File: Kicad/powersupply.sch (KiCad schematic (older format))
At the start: 19 parts, among them J801 Jack 2/6.3mm, Q801 BC546, Q802 BC556, U801 DC-DC Module, U802 MAX1615, U803 TLV1117 3.3V 1A

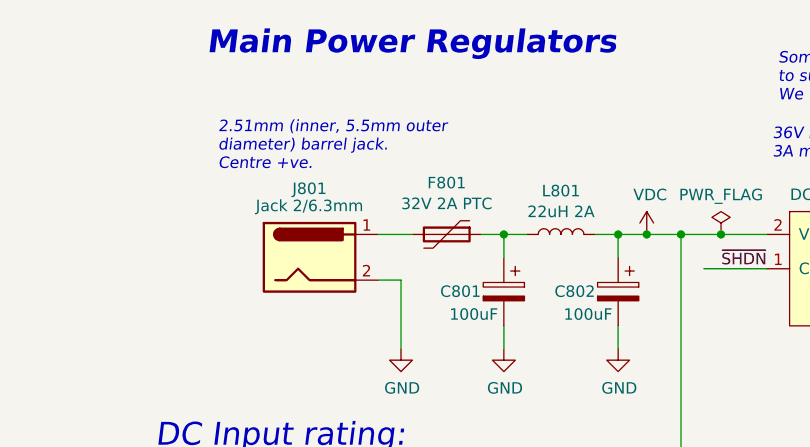
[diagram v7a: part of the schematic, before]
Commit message: Update component values.
Tolerance and Voltage are set to the minimum acceptable. The selected
parts can be better, where a better part is cheaper or has
better availability.

Also dropped R2R DAC tolerance to 1% - 0.5% was overkill. The output
resistor had the wrong value too, which is fixed.
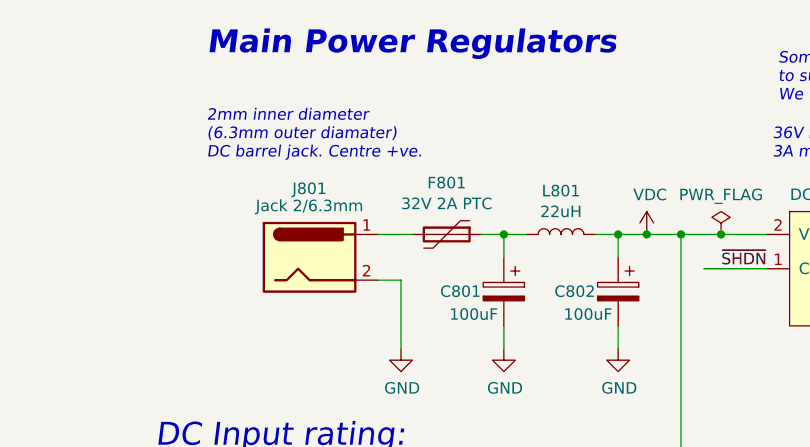
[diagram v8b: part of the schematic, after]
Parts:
- C801, C802: Tolerance (none) -> 20%
- C803: Tolerance (none) -> X5R
- C804, C806, C808: Tolerance (none) -> X5R; Voltage (none) -> 16V
- C805, C807: Tolerance (none) -> X5R; Voltage (none) -> 10V
- L801: value 22uH 2A -> 22uH; Mouser (none) -> 580-13R223C
- Q801: Mouser (none) -> 512-BC546CTA
- Q802: Mouser (none) -> 512-BC556BTF
- R801, R802, R803: Tolerance (none) -> 1%
- U803: Digikey 296-28778-1-ND -> (none); Mouser 595-TLV1117LV33DCYR -> (none)
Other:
- note added: "2mm inner diameter\n(6.3mm outer diamater)\nDC barrel jack. Centre +ve."
- note removed: "2.51mm (inner, 5.5mm outer\ndiameter) barrel jack.\nCentre +ve."
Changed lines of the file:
@@
 Comment4 ""
 $EndDescr
-Text Notes 1975 1850 0    50   Italic 0
-2.51mm (inner, 5.5mm outer\ndiameter) barrel jack.\nCentre +ve.
+Text Notes 1925 1800 0    50   Italic 0
+2mm inner diameter\n(6.3mm outer diamater)\nDC barrel jack. Centre +ve.
 Text Notes 8525 4075 0    50   Italic 0
 Most of our board runs on 3.3V. We expect\nto draw around 100 mA from this 1A linear\nregulator.\n\nNorm. power wasted: (5V - 3.3V) * 0.1A = 0.17W\nMax power wasted: (5V - 3.3V) * 1A = 1.7W\n\nThe LDO is 50 °C/W so at max power,\nit's 85 °C over ambient. Probably best\nto use a heatsink if you want to pull\nover about 250 mA. Or replace with a\n3-terminal switching PSU module.
@@
 F 3 "http://www.ti.com/general/docs/suppproductinfo.tsp?distId=10&gotoUrl=http%3A%2F%2Fwww.ti.com%2Flit%2Fgpn%2Ftlv1117lv" H 7625 3275 50  0001 C CNN
 F 4 "0" H 7525 3525 50  0001 C CNN "DNP"
-F 5 "296-28778-1-ND" H 7525 3525 50  0001 C CNN "Digikey"
+F 5 "~" H 7525 3525 50  0001 C CNN "Digikey"
 F 6 "CPL-REG-LIN-3.3V-1A" H 7525 3525 50  0001 C CNN "MPN"
 F 7 "CPL" H 7525 3525 50  0001 C CNN "Manufacturer"
-F 8 "595-TLV1117LV33DCYR" H 7525 3525 50  0001 C CNN "Mouser"
+F 8 "~" H 7525 3525 50  0001 C CNN "Mouser"
 F 9 "C6186" H 7525 3525 50  0001 C CNN "LCSC Part#"
+F 10 "~" H 7525 3525 50  0001 C CNN "Tolerance"
+F 11 "~" H 7525 3525 50  0001 C CNN "Voltage"
 	1    7525 3525
 	1    0    0    -1
@@
 F 3 "~" H 7875 3775 50  0001 C CNN
 F 4 "0" H 7875 3775 50  0001 C CNN "DNP"
-F 5 "" H 7875 3775 50  0001 C CNN "Digikey"
+F 5 "~" H 7875 3775 50  0001 C CNN "Digikey"
 F 6 "CPL-CAP-X7R-0805-1UF-25V" H 7875 3775 50  0001 C CNN "MPN"
 F 7 "CPL" H 7875 3775 50  0001 C CNN "Manufacturer"
 F 8 "C28323" H 7875 3775 50  0001 C CNN "LCSC Part#"
+F 9 "X5R" H 7875 3775 50  0001 C CNN "Tolerance"
+F 10 "10V" H 7875 3775 50  0001 C CNN "Voltage"
+F 11 "~" H 7875 3775 50  0001 C CNN "Mouser"
 	1    7875 3775
 	1    0    0    -1
@@
 F 8 "530-0ZRS0200FF1E" H 2975 2125 50  0001 C CNN "Mouser"
 F 9 "~" H 2975 2125 50  0001 C CNN "LCSC Part#"
+F 10 "~" H 2975 2125 50  0001 C CNN "Tolerance"
+F 11 "~" H 2975 2125 50  0001 C CNN "Voltage"
 	1    2975 2125
 	0    1    1    0
@@
 F 8 "700-MAX1615EUKT" H 4725 3975 50  0001 C CNN "Mouser"
 F 9 "C52770" H 4725 3975 50  0001 C CNN "LCSC Part#"
+F 10 "~" H 4725 3975 50  0001 C CNN "Tolerance"
+F 11 "~" H 4725 3975 50  0001 C CNN "Voltage"
 	1    4725 3975
 	1    0    0    -1
@@
 F 3 "~" H 4000 4275 50  0001 C CNN
 F 4 "0" H 4000 4275 50  0001 C CNN "DNP"
-F 5 "" H 4000 4275 50  0001 C CNN "Digikey"
+F 5 "~" H 4000 4275 50  0001 C CNN "Digikey"
 F 6 "CPL-CAP-X7R-0805-100NF-50V" H 4000 4275 50  0001 C CNN "MPN"
 F 7 "CPL" H 4000 4275 50  0001 C CNN "Manufacturer"
 F 8 "C49678" H 4000 4275 50  0001 C CNN "LCSC Part#"
 F 9 "50V" H 4000 4275 50  0001 C CNN "Voltage"
+F 10 "X5R" H 4000 4275 50  0001 C CNN "Tolerance"
+F 11 "~" H 4000 4275 50  0001 C CNN "Mouser"
 	1    4000 4275
 	1    0    0    -1
@@
 F 3 "~" H 7175 3775 50  0001 C CNN
 F 4 "0" H 7175 3775 50  0001 C CNN "DNP"
-F 5 "" H 7175 3775 50  0001 C CNN "Digikey"
+F 5 "~" H 7175 3775 50  0001 C CNN "Digikey"
 F 6 "CPL-CAP-X7R-0805-100NF-50V" H 7175 3775 50  0001 C CNN "MPN"
 F 7 "CPL" H 7175 3775 50  0001 C CNN "Manufacturer"
-F 8 "" H 7175 3775 50  0001 C CNN "Mouser"
+F 8 "~" H 7175 3775 50  0001 C CNN "Mouser"
 F 9 "C49678" H 7175 3775 50  0001 C CNN "LCSC Part#"
+F 10 "X5R" H 7175 3775 50  0001 C CNN "Tolerance"
+F 11 "16V" H 7175 3775 50  0001 C CNN "Voltage"
 	1    7175 3775
 	-1   0    0    -1
@@
 F 3 "~" H 5275 2375 50  0001 C CNN
 F 4 "0" H 5275 2375 50  0001 C CNN "DNP"
-F 5 "" H 5275 2375 50  0001 C CNN "Digikey"
+F 5 "~" H 5275 2375 50  0001 C CNN "Digikey"
 F 6 "CPL-CAP-X5R-0805-10UF-16V" H 5275 2375 50  0001 C CNN "MPN"
 F 7 "CPL" H 5275 2375 50  0001 C CNN "Manufacturer"
 F 8 "C15850" H 5275 2375 50  0001 C CNN "LCSC Part#"
+F 9 "X5R" H 5275 2375 50  0001 C CNN "Tolerance"
+F 10 "16V" H 5275 2375 50  0001 C CNN "Voltage"
+F 11 "~" H 5275 2375 50  0001 C CNN "Mouser"
 	1    5275 2375
 	1    0    0    -1
@@
 P 3475 2125
 F 0 "L801" V 3665 2125 50  0000 C CNN
-F 1 "22uH 2A" V 3574 2125 50  0000 C CNN
+F 1 "22uH" V 3574 2125 50  0000 C CNN
 F 2 "Inductor_THT:L_Radial_D9.5mm_P5.00mm_Fastron_07HVP" H 3475 2125 50  0001 C CNN
 F 3 "https://www.murata-ps.com/pub/data/magnetics/kmp_1300r.pdf" H 3475 2125 50  0001 C CNN
@@
 F 6 "Murata" V 3475 2125 50  0001 C CNN "Manufacturer"
 F 7 "811-2042-ND" V 3475 2125 50  0001 C CNN "Digikey"
-F 8 "" H 3475 2125 50  0001 C CNN "Mouser"
+F 8 "580-13R223C" H 3475 2125 50  0001 C CNN "Mouser"
 F 9 "~" H 3475 2125 50  0001 C CNN "LCSC Part#"
+F 10 "~" H 3475 2125 50  0001 C CNN "Tolerance"
+F 11 "~" H 3475 2125 50  0001 C CNN "Voltage"
 	1    3475 2125
 	0    -1   -1   0
@@
 F 3 "~" H 3225 2375 50  0001 C CNN
 F 4 "0" H 3225 2375 50  0001 C CNN "DNP"
-F 5 "" H 3225 2375 50  0001 C CNN "Digikey"
+F 5 "~" H 3225 2375 50  0001 C CNN "Digikey"
 F 6 "CPL-CAP-ALU-RAD-100UF-50V" H 3225 2375 50  0001 C CNN "MPN"
 F 7 "CPL" H 3225 2375 50  0001 C CNN "Manufacturer"
-F 8 "" H 3225 2375 50  0001 C CNN "Mouser"
+F 8 "~" H 3225 2375 50  0001 C CNN "Mouser"
 F 9 "~" H 3225 2375 50  0001 C CNN "LCSC Part#"
 F 10 "50V" H 3225 2375 50  0001 C CNN "Voltage"
+F 11 "20%" H 3225 2375 50  0001 C CNN "Tolerance"
 	1    3225 2375
 	-1   0    0    -1
@@
 F 3 "~" H 3725 2375 50  0001 C CNN
 F 4 "0" H 3725 2375 50  0001 C CNN "DNP"
-F 5 "" H 3725 2375 50  0001 C CNN "Digikey"
+F 5 "~" H 3725 2375 50  0001 C CNN "Digikey"
 F 6 "CPL-CAP-ALU-RAD-100UF-50V" H 3725 2375 50  0001 C CNN "MPN"
 F 7 "CPL" H 3725 2375 50  0001 C CNN "Manufacturer"
-F 8 "" H 3725 2375 50  0001 C CNN "Mouser"
+F 8 "~" H 3725 2375 50  0001 C CNN "Mouser"
 F 9 "~" H 3725 2375 50  0001 C CNN "LCSC Part#"
 F 10 "50V" H 3725 2375 50  0001 C CNN "Voltage"
+F 11 "20%" H 3725 2375 50  0001 C CNN "Tolerance"
 	1    3725 2375
 	-1   0    0    -1
@@
 F 8 "490-PJ-063AH" H 2375 2225 50  0001 C CNN "Mouser"
 F 9 "~" H 2375 2225 50  0001 C CNN "LCSC Part#"
+F 10 "~" H 2375 2225 50  0001 C CNN "Tolerance"
+F 11 "~" H 2375 2225 50  0001 C CNN "Voltage"
 	1    2375 2225
 	1    0    0    -1
@@
 F 7 "K7805-3AR3" H 4725 1975 50  0001 C CNN "MPN"
 F 8 "~" H 4725 1975 50  0001 C CNN "LCSC Part#"
+F 9 "~" H 4725 1975 50  0001 C CNN "Mouser"
+F 10 "~" H 4725 1975 50  0001 C CNN "Tolerance"
+F 11 "~" H 4725 1975 50  0001 C CNN "Voltage"
 	1    4725 1975
 	1    0    0    -1
@@
 F 3 "~" H 5425 4275 50  0001 C CNN
 F 4 "0" H 5425 4275 50  0001 C CNN "DNP"
-F 5 "" H 5425 4275 50  0001 C CNN "Digikey"
+F 5 "~" H 5425 4275 50  0001 C CNN "Digikey"
 F 6 "CPL-CAP-X5R-0805-4.7UF-25V" H 5425 4275 50  0001 C CNN "MPN"
 F 7 "CPL" H 5425 4275 50  0001 C CNN "Manufacturer"
 F 8 "C1779" H 5425 4275 50  0001 C CNN "LCSC Part#"
+F 9 "X5R" H 5425 4275 50  0001 C CNN "Tolerance"
+F 10 "10V" H 5425 4275 50  0001 C CNN "Voltage"
+F 11 "~" H 5425 4275 50  0001 C CNN "Mouser"
 	1    5425 4275
 	1    0    0    -1
@@
 F 7 "0" H 1925 5900 50  0001 C CNN "DNP"
 F 8 "~" H 1925 5900 50  0001 C CNN "LCSC Part#"
+F 9 "512-BC546CTA" H 1925 5900 50  0001 C CNN "Mouser"
+F 10 "~" H 1925 5900 50  0001 C CNN "Tolerance"
+F 11 "~" H 1925 5900 50  0001 C CNN "Voltage"
 	1    1925 5900
 	1    0    0    -1
@@
 F 7 "0" H 2475 5550 50  0001 C CNN "DNP"
 F 8 "~" H 2475 5550 50  0001 C CNN "LCSC Part#"
+F 9 "512-BC556BTF" H 2475 5550 50  0001 C CNN "Mouser"
+F 10 "~" H 2475 5550 50  0001 C CNN "Tolerance"
+F 11 "~" H 2475 5550 50  0001 C CNN "Voltage"
 	1    2475 5550
 	1    0    0    1
@@
 F 3 "~" H 1550 5900 50  0001 C CNN
 F 4 "0" H 1550 5900 50  0001 C CNN "DNP"
-F 5 "" H 1550 5900 50  0001 C CNN "Digikey"
+F 5 "~" H 1550 5900 50  0001 C CNN "Digikey"
 F 6 "CPL-RES-0805-10K-0.125W" H 1550 5900 50  0001 C CNN "MPN"
 F 7 "CPL" H 1550 5900 50  0001 C CNN "Manufacturer"
 F 8 "C17414" H 1550 5900 50  0001 C CNN "LCSC Part#"
+F 9 "1%" H 1550 5900 50  0001 C CNN "Tolerance"
+F 10 "~" H 1550 5900 50  0001 C CNN "Mouser"
+F 11 "~" H 1550 5900 50  0001 C CNN "Voltage"
 	1    1550 5900
 	0    1    -1   0
@@
 F 3 "~" H 2025 5300 50  0001 C CNN
 F 4 "0" H 2025 5300 50  0001 C CNN "DNP"
-F 5 "" H 2025 5300 50  0001 C CNN "Digikey"
+F 5 "~" H 2025 5300 50  0001 C CNN "Digikey"
 F 6 "CPL-RES-0805-10K-0.125W" H 2025 5300 50  0001 C CNN "MPN"
 F 7 "CPL" H 2025 5300 50  0001 C CNN "Manufacturer"
 F 8 "C17414" H 2025 5300 50  0001 C CNN "LCSC Part#"
+F 9 "1%" H 2025 5300 50  0001 C CNN "Tolerance"
+F 10 "~" H 2025 5300 50  0001 C CNN "Mouser"
+F 11 "~" H 2025 5300 50  0001 C CNN "Voltage"
 	1    2025 5300
 	-1   0    0    -1
@@
 F 3 "~" H 2575 6150 50  0001 C CNN
 F 4 "0" H 2575 6150 50  0001 C CNN "DNP"
-F 5 "" H 2575 6150 50  0001 C CNN "Digikey"
+F 5 "~" H 2575 6150 50  0001 C CNN "Digikey"
 F 6 "CPL-RES-0805-10K-0.125W" H 2575 6150 50  0001 C CNN "MPN"
 F 7 "CPL" H 2575 6150 50  0001 C CNN "Manufacturer"
 F 8 "C17414" H 2575 6150 50  0001 C CNN "LCSC Part#"
+F 9 "1%" H 2575 6150 50  0001 C CNN "Tolerance"
+F 10 "~" H 2575 6150 50  0001 C CNN "Mouser"
+F 11 "~" H 2575 6150 50  0001 C CNN "Voltage"
 	1    2575 6150
 	-1   0    0    -1
@@
 F 3 "~" H 5850 2375 50  0001 C CNN
 F 4 "0" H 5850 2375 50  0001 C CNN "DNP"
-F 5 "" H 5850 2375 50  0001 C CNN "Digikey"
+F 5 "~" H 5850 2375 50  0001 C CNN "Digikey"
 F 6 "CPL-CAP-X5R-0805-10UF-16V" H 5850 2375 50  0001 C CNN "MPN"
 F 7 "CPL" H 5850 2375 50  0001 C CNN "Manufacturer"
 F 8 "C15850" H 5850 2375 50  0001 C CNN "LCSC Part#"
+F 9 "X5R" H 5850 2375 50  0001 C CNN "Tolerance"
+F 10 "16V" H 5850 2375 50  0001 C CNN "Voltage"
+F 11 "~" H 5850 2375 50  0001 C CNN "Mouser"
 	1    5850 2375
 	1    0    0    -1
